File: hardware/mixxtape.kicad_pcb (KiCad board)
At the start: 2 copper layers, 99.5 x 63.5 mm, 71 parts, among them J1 USB-C_SMD-TYPE-C-31-M-12_1, J4 TF-SMD_TF-01A, J5 PROG_JIG, SW1 SW-SMD_4P-L5.1-W5.1-P3.70-LS6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, SW2 SW-SMD_4P-L5.1-W5.1-P3.70-LS6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, SW3 SW-SMD_4P-L5.1-W5.1-P3.70-LS6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, SW4 SW-SMD_4P-L5.1-W5.1-P3.70-LS6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, U1 WIFI-SMD_ESP32-WROOM-32E, U2 LGA-8_L4.0-W3.0-R_WMM7040DT0, U3 SOIC-8_L5.3-W5.3-P1.27-LS8.0-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, U4 SOT-223-3_L6.5-W3.4-P2.30-LS7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, U8 SOT-23-5_L3.0-W1.7-P0.95-LS2.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

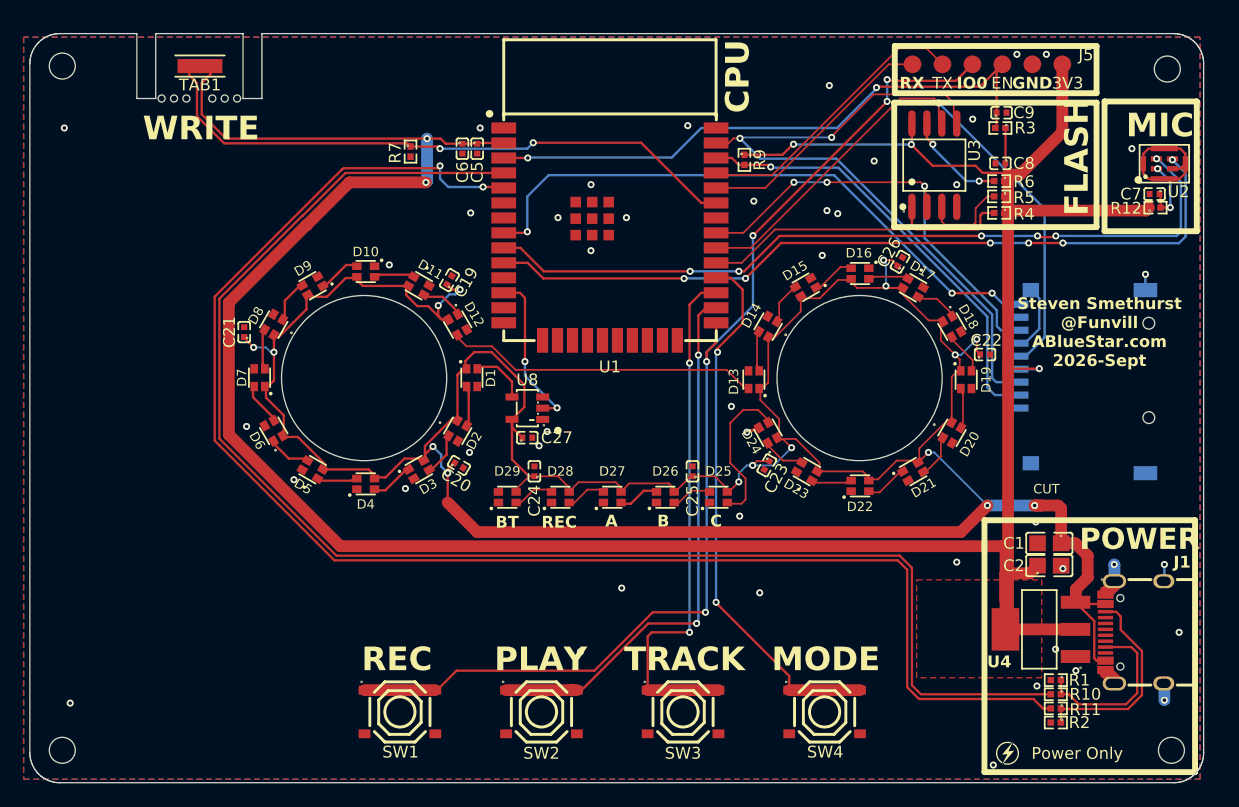
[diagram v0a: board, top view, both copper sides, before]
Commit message: hardware: restore the B-side artwork, and centre its bleed this time
The peony was removed in ee24c0e. Restored from e15b369 verbatim - 2.16 MB,
81,406 points across 193 B.SilkS shapes - with one change: it moves +0.382 mm
in x.

It had been drawn to the ORIGINAL 100.33 mm outline, and the board was later
trimmed to 99.50 mm from the LEFT. So at its old position the artwork hung
0.806 mm off the left edge and only 0.042 mm off the right: the fab's clip
took a visible bite out of one side of the design while the other side barely
bled at all. Shifting right by half the difference splits the 0.848 mm of
excess evenly - 0.420 mm of bleed left, 0.428 mm right - which is what a
full-bleed design actually wants. silk_edge_clearance warnings drop from the
original 54 to 28 as a side effect.

B_Silkscreen.gbo is back to 2,106,867 bytes and the Gerber zip to 0.96 MB.

DRC 0 errors, 0 unconnected. ERC 0 errors, 0 warnings. Warnings rise 60 -> 157,
all silkscreen and all from the artwork: the export passes
--subtract-soldermask, so silk is clipped by the mask and no ink reaches a pad
or an exposed via annulus.

Note docs/b-side-silkscreen-brief.html still briefs a designer to replace this
placeholder.

Co-Authored-By: Claude Opus 5 <noreply@anthropic.com>
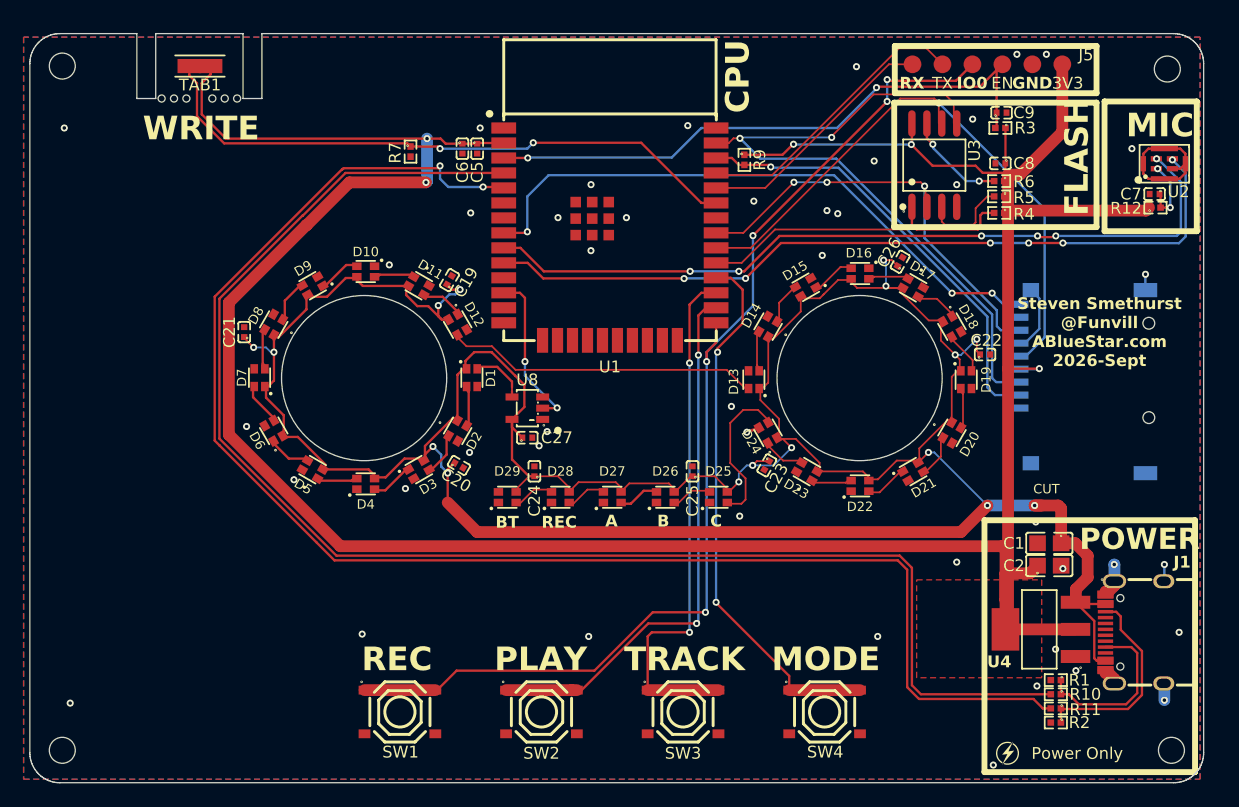
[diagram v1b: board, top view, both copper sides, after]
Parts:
- added G***: LOGO, LOGO, B.Cu at (80.6, 61.7)
